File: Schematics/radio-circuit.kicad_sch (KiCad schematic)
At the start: 36 parts, among them J1 USB_B_Micro, J2 STDC14, J3 0, U1 USBLC6-2SC6, U2 LD39015M33R, U3 STM32F042C6T6, U4 Si4705-D60-GM, Y1 SG-3030CM

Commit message: Took the new footprint into use
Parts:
- U4: footprint Package_DFN_QFN:SiliconLabs_QFN-20-1EP_3x3mm_P0.5mm_EP1.8x1.8mm -> Local:Skyworks_QFN-20-1EP_3x3mm_P0.5mm_EP1.8x1.8mm
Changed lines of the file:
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@@
 			)
 		)
-		(property "Footprint" "Package_DFN_QFN:SiliconLabs_QFN-20-1EP_3x3mm_P0.5mm_EP1.8x1.8mm"
+		(property "Footprint" "Local:Skyworks_QFN-20-1EP_3x3mm_P0.5mm_EP1.8x1.8mm"
 			(at 195.58 66.04 0)
 			(hide yes)

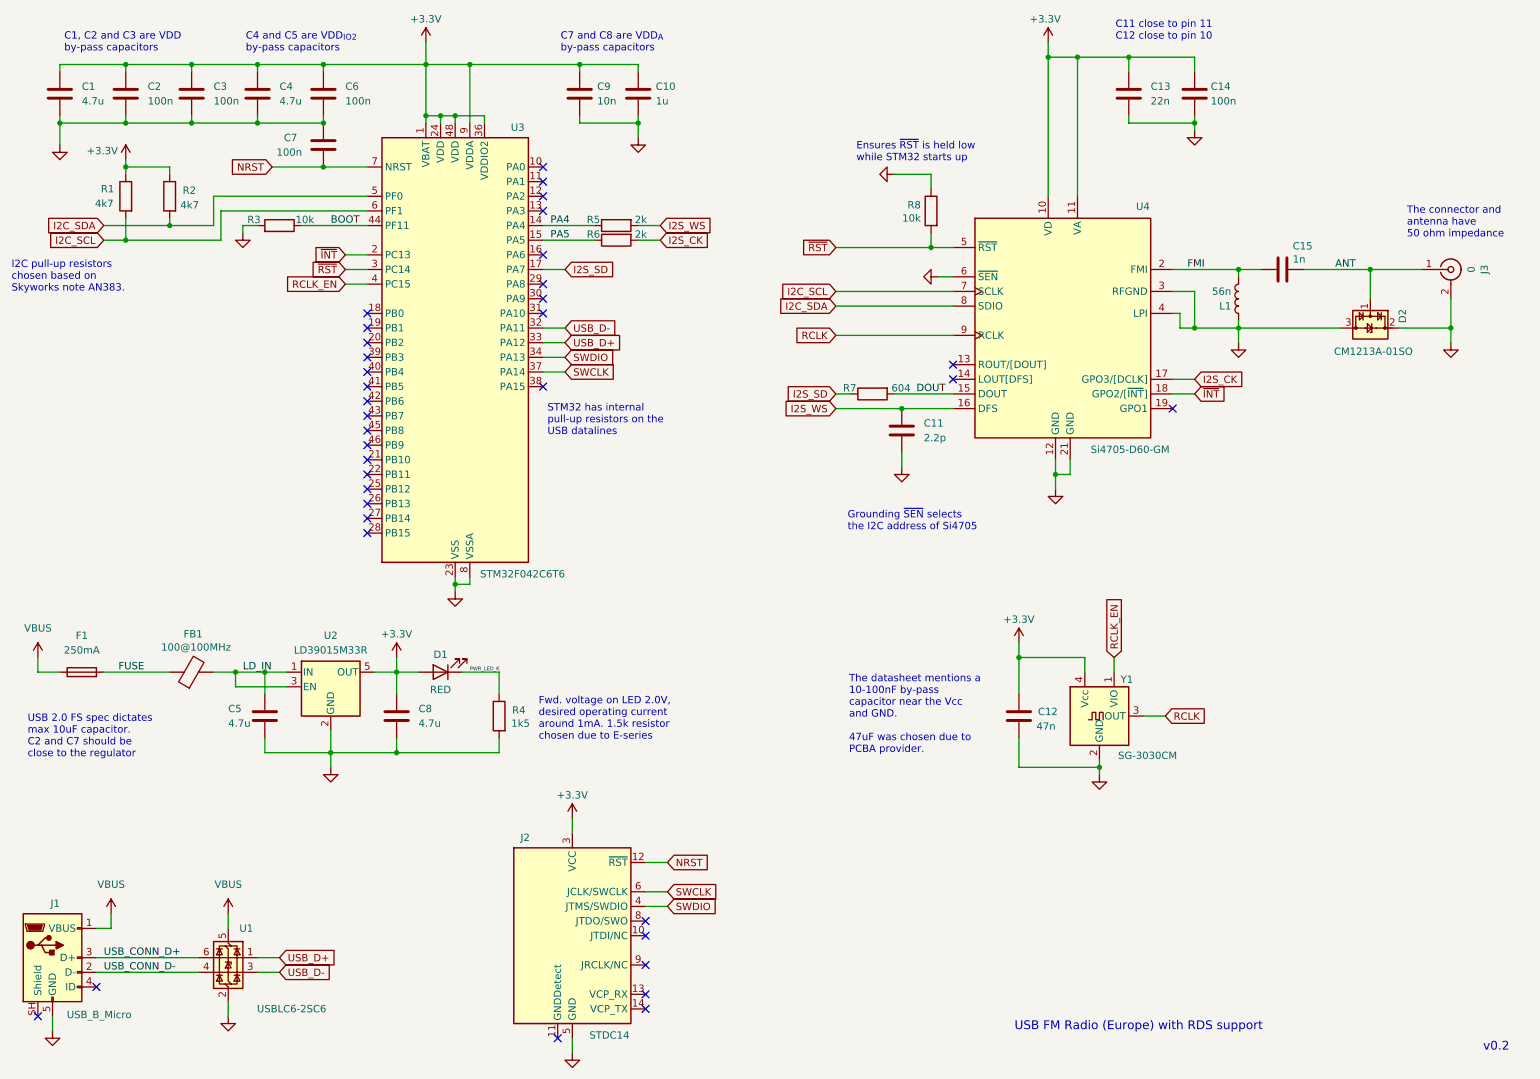
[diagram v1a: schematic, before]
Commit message: New PCB version with STM32F042F6Px
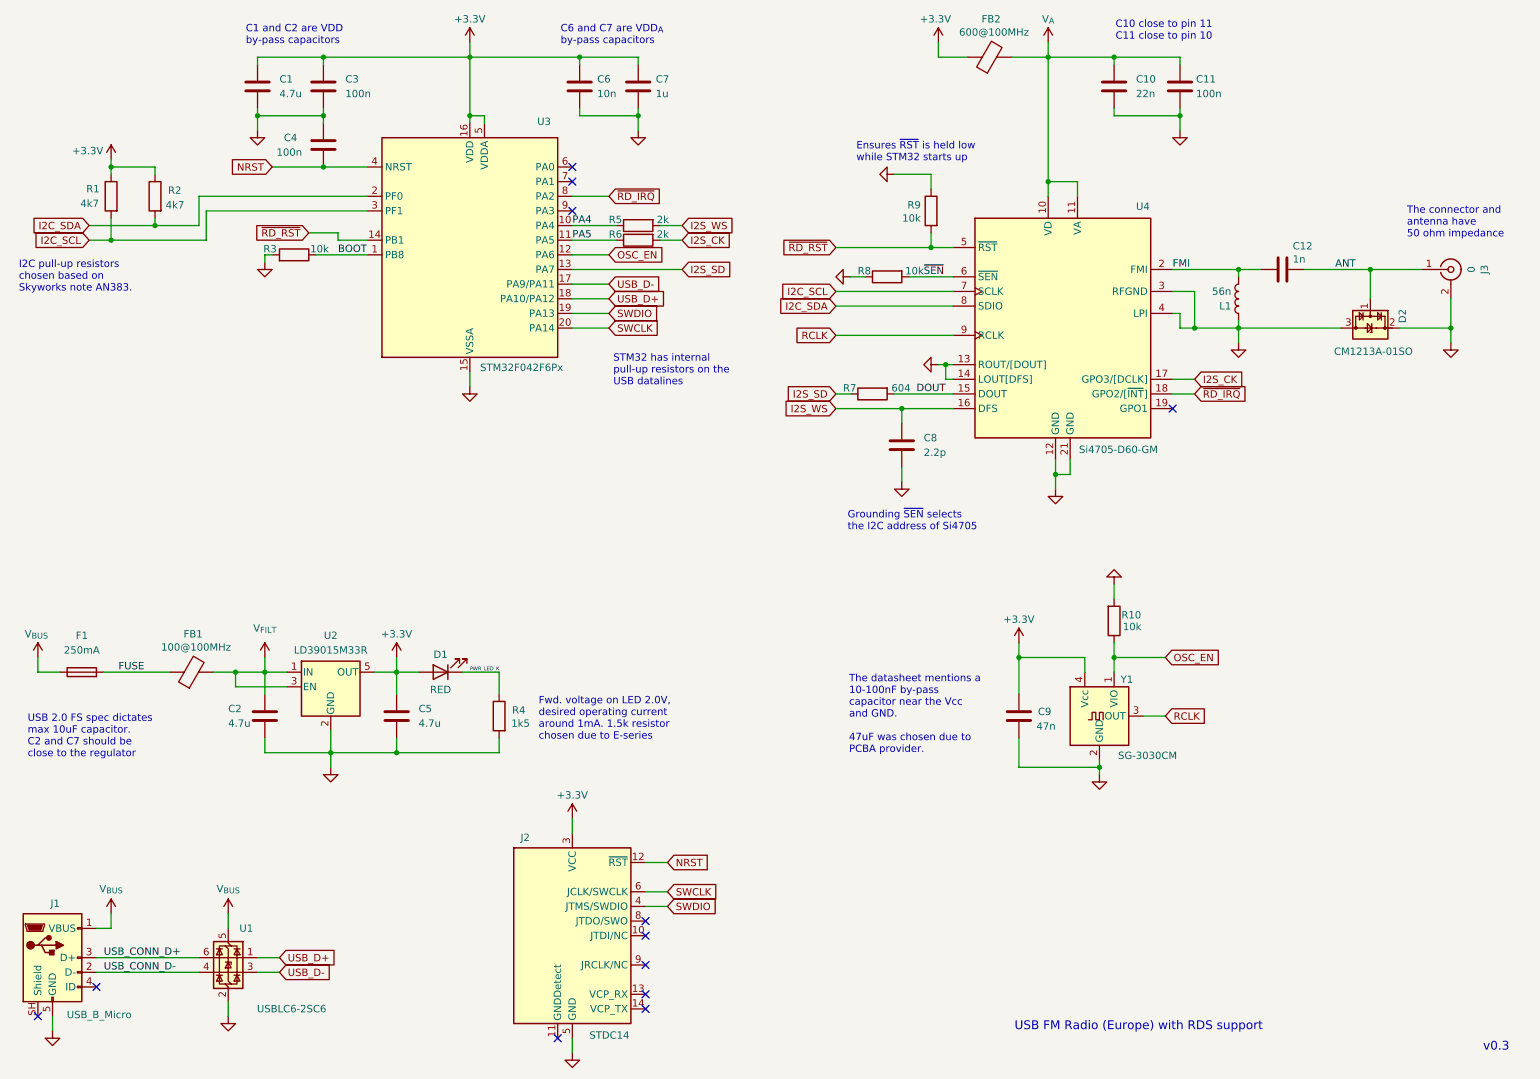
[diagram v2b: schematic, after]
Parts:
- removed C1: 4.7u, Capacitor_SMD:C_0603_1608Metric, symbol Device:C
- removed C2, C3: 100n, Capacitor_SMD:C_0402_1005Metric, symbol Device:C
- removed U3: STM32F042C6T6, Package_QFP:LQFP-48_7x7mm_P0.5mm, symbol MCU_ST_STM32F0:STM32F042C6Tx
- added FB2: 600@100MHz, Inductor_SMD:L_0402_1005Metric, symbol Device:FerriteBead
- added R10, R8: 10k, Resistor_SMD:R_0402_1005Metric, symbol Device:R
- added U3: STM32F042F6Px, Package_SO:TSSOP-20_4.4x6.5mm_P0.65mm, symbol MCU_ST_STM32F0:STM32F042F6Px
- renumbered C4 to C1, C13 to C10, C14 to C11, C15 to C12, C5 to C2, C6 to C3, C7 to C4, C8 to C5, C9 to C6, C10 to C7, C11 to C8, C12 to C9, R8 to R9
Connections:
- net +3.3V: now also FB2.1, U3.16 (VDD), U3.5 (VDDA); no longer C10.1, C11.1, U4.10 (VD), U4.11 (VA)
- net BOOT: now also U3.1 (PB8)
- net GND: now also U4.13 (ROUT/[DOUT]), U4.14 (LOUT[DFS]), R10.2, R8.1, U3.15 (VSSA); no longer U4.6 (~{SEN})
- net I2C_SCL: now also U3.3 (PF1)
- net I2C_SDA: now also U3.2 (PF0)
- net I2S_SD: now also U3.13 (PA7)
- net NRST: now also U3.4 (NRST)
- net PA4: now also U3.10 (PA4)
- net PA5: now also U3.11 (PA5)
- net SWCLK: now also U3.20 (PA14)
- net SWDIO: now also U3.19 (PA13)
- net USB_D+: now also U3.18 (PA10/PA12)
- net USB_D-: now also U3.17 (PA9/PA11)
- net LD_IN renamed V_{FILT}
- net RCLK_EN renamed OSC_EN
- net OSC_EN: now also R10.1, U3.12 (PA6)
- net VBUS renamed V_{BUS}
- net ~{INT} renamed ~{RD_IRQ}
- net ~{RD_IRQ}: now also U3.8 (PA2)
- net ~{RST} renamed ~{RD_RST}
- net ~{RD_RST}: now also U3.14 (PB1)
- new net  ~{SEN}: R8.2, U4.6 (~{SEN})
- new net V_{A}: C10.1, C11.1, FB2.2, U4.10 (VD), U4.11 (VA)
- no-connect marks 36 -> 12
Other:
- note added: "C1 and C2 are VDD by-pass capacitors"
- note added: "C10 close to pin 11 C11 close to pin 10"
- note added: "C6 and C7 are VDD_{A} by-pass capacitors"
- note added: "v0.3"
- note removed: "C1, C2 and C3 are VDD by-pass capacitors"
- note removed: "C11 close to pin 11 C12 close to pin 10"
- note removed: "C4 and C5 are VDD_{IO2} by-pass capacitors"
- note removed: "C7 and C8 are VDD_{A} by-pass capacitors"
- note removed: "v0.2"
- moved on the sheet: C1, C10, C11, C3, C6, C7, C8, R1, R2, R3, R5, R6

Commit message: Took connector into use, and started a new PCB layout
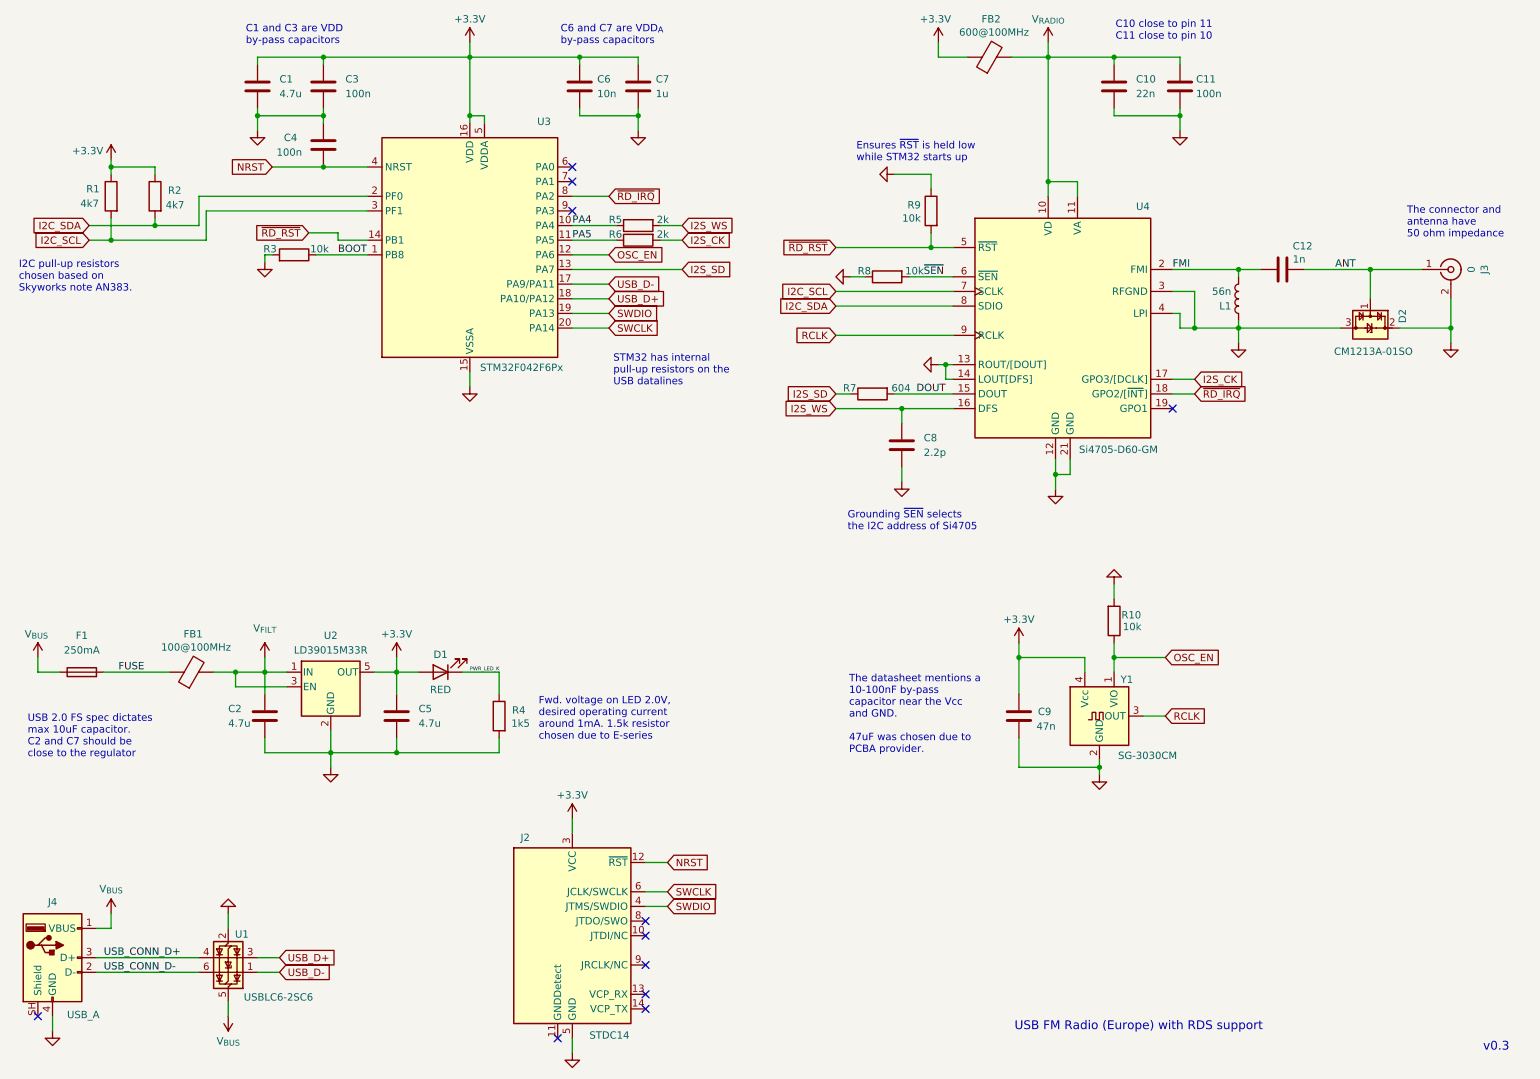
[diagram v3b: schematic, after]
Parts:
- removed J1: USB_B_Micro, Connector_USB:USB_Micro-B_Molex_47346-0001, symbol Connector:USB_B_Micro
- added J4: USB_A, Local:USB_A_Molex_48037-2200_Horizontal, symbol Connector:USB_A
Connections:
- net GND: now also J4.4 (GND)
- net USB_CONN_D+: now also U1.4 (I/O2), J4.3 (D+); no longer U1.6 (I/O1)
- net USB_CONN_D-: now also U1.6 (I/O1), J4.2 (D-); no longer U1.4 (I/O2)
- net USB_D+: now also U1.3 (I/O2); no longer U1.1 (I/O1)
- net USB_D-: now also U1.1 (I/O1); no longer U1.3 (I/O2)
- net V_{BUS}: now also J4.1 (VBUS)
- net V_{A} renamed V_{RADIO}
- no-connect marks 12 -> 11
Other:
- note added: "C1 and C3 are VDD by-pass capacitors"
- note removed: "C1 and C2 are VDD by-pass capacitors"
- moved on the sheet: U1

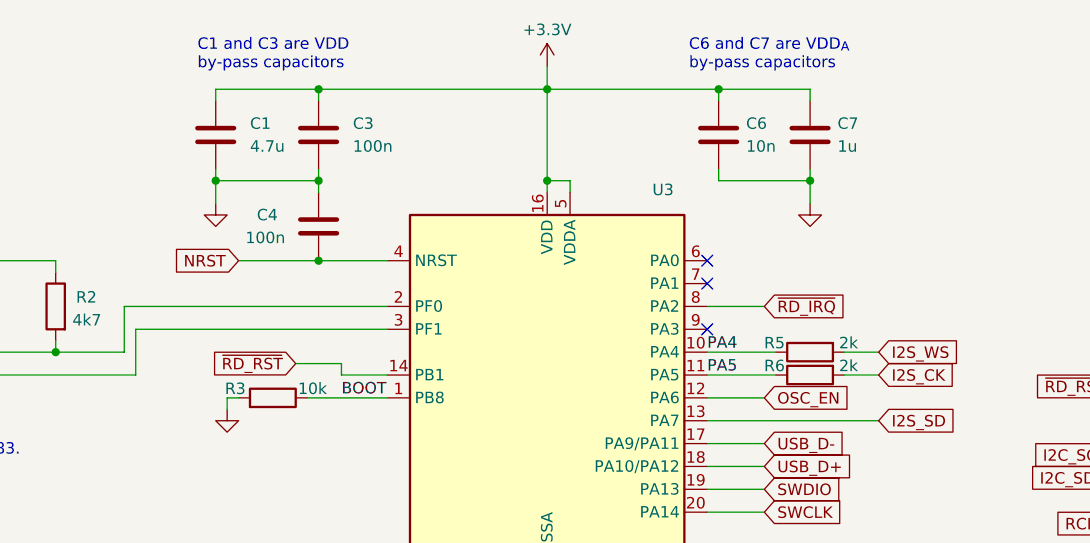
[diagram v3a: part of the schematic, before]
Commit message: Switched radio GPIOs to the same side, and updated some labels
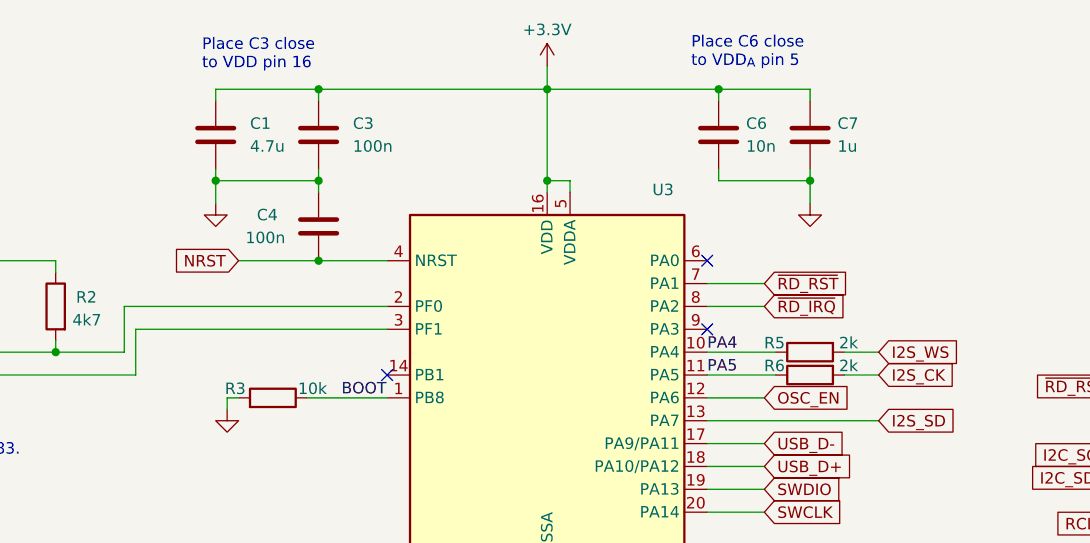
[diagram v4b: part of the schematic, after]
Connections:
- net ~{RD_RST}: now also U3.7 (PA1); no longer U3.14 (PB1)
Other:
- note added: "Place C3 close to VDD pin 16"
- note added: "Place C6 close to VDD_{A} pin 5"
- note removed: "C1 and C3 are VDD by-pass capacitors"
- note removed: "C6 and C7 are VDD_{A} by-pass capacitors"
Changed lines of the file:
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@@
 		)
 	)
-	(text "C6 and C7 are VDD_{A}\nby-pass capacitors"
+	(text "Place C6 close\nto VDD_{A} pin 5"
 		(exclude_from_sim no)
-		(at 108.458 17.78 0)
+		(at 108.712 17.526 0)
 		(effects
 			(font
@@
 		)
 	)
-	(text "C1 and C3 are VDD\nby-pass capacitors"
+	(text "Place C3 close\nto VDD pin 16"
 		(exclude_from_sim no)
-		(at 53.848 17.78 0)
+		(at 54.356 17.78 0)
 		(effects
 			(font
@@
 	)
 	(no_connect
-		(at 110.49 43.18)
-	)
-	(no_connect
 		(at 107.95 191.77)
 	)
@@
 	)
 	(no_connect
+		(at 74.93 53.34)
+	)
+	(no_connect
 		(at 110.49 40.64)
 	)
@@
 	(wire
 		(pts
-			(xy 74.93 53.34) (xy 69.85 53.34)
-		)
-		(stroke
-			(width 0)
-			(type default)
-		)
-	)
-	(wire
-		(pts
 			(xy 196.85 93.98) (xy 194.31 93.98)
 		)
@@
 	(wire
 		(pts
+			(xy 110.49 43.18) (xy 116.84 43.18)
+		)
+		(stroke
+			(width 0)
+			(type default)
+		)
+	)
+	(wire
+		(pts
 			(xy 226.06 68.58) (xy 226.06 71.12)
 		)
@@
 	(wire
 		(pts
-			(xy 69.85 53.34) (xy 69.85 52.07)
-		)
-		(stroke
-			(width 0)
-			(type default)
-		)
-	)
-	(wire
-		(pts
 			(xy 226.06 68.58) (xy 243.84 68.58)
 		)
@@
 		(pts
 			(xy 214.63 58.42) (xy 226.06 58.42)
-		)
-		(stroke
-			(width 0)
-			(type default)
-		)
-	)
-	(wire
-		(pts
-			(xy 69.85 52.07) (xy 64.77 52.07)
 		)
 		(stroke
@@
 	(global_label "~{RD_RST}"
 		(shape input)
-		(at 64.77 52.07 180)
+		(at 116.84 43.18 0)
 		(fields_autoplaced yes)
 		(effects
@@
 				(size 1.27 1.27)
 			)
-			(justify right)
+			(justify left)
 		)
 		(property "Intersheetrefs" "${INTERSHEET_REFS}"
-			(at 54.8301 52.07 0)
+			(at 126.7799 43.18 0)
 			(hide yes)
 			(show_name no)
@@
 					(size 1.27 1.27)
 				)
-				(justify right)
-			)
-		)
+				(justify left)
+			)
+		)
